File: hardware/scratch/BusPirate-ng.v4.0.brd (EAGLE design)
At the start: 100 x 50 mm, 136 parts, among them CON1 CON-USB-F-MICRO-B, IC10 74LVC1G07DBV, IC11 IC_BUFF_SN74LVC1T45DBV, IC12 74LVC1G07DBV, IC13 IC_BUFF_SN74LVC1T45DBV, IC14 74LVC1G07DBV, IC15 IC_BUFF_SN74LVC1T45DBV, IC16 74LVC1G07DBV, IC17 IC_BUFF_SN74LVC1T45DBV, IC2 IC_MEM_23LC1024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

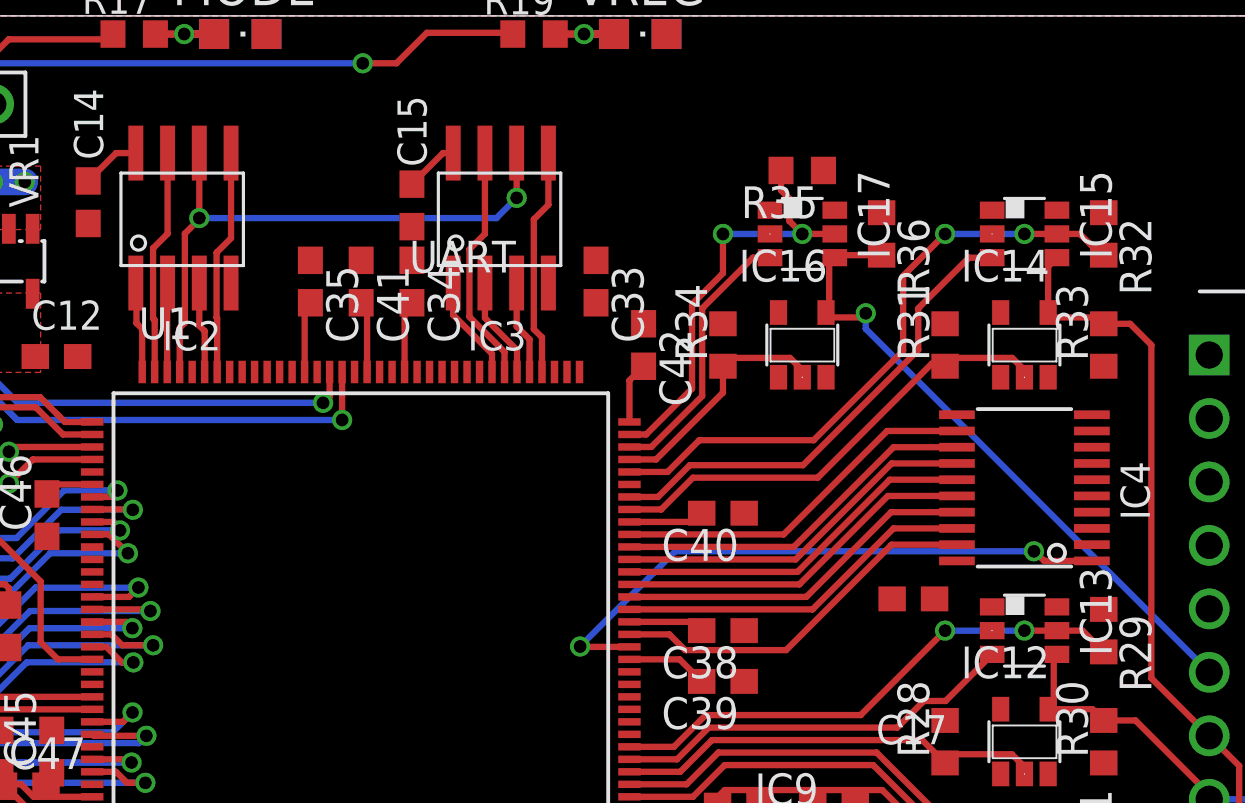
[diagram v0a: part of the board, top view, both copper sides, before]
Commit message: Renamed nets name and wire missing connection -renamed SRAM nets -renamed LATCH nets -wired FSMC control pins. FSMC_NOE_OE, FSMC_NWE_WE and FSMC_NE3_CE to FPGA 11, 12 and 22. -wired PWM pin PC6 (TIM8_CH1/TIM3_CH1) to FPGA 21/GBIN6
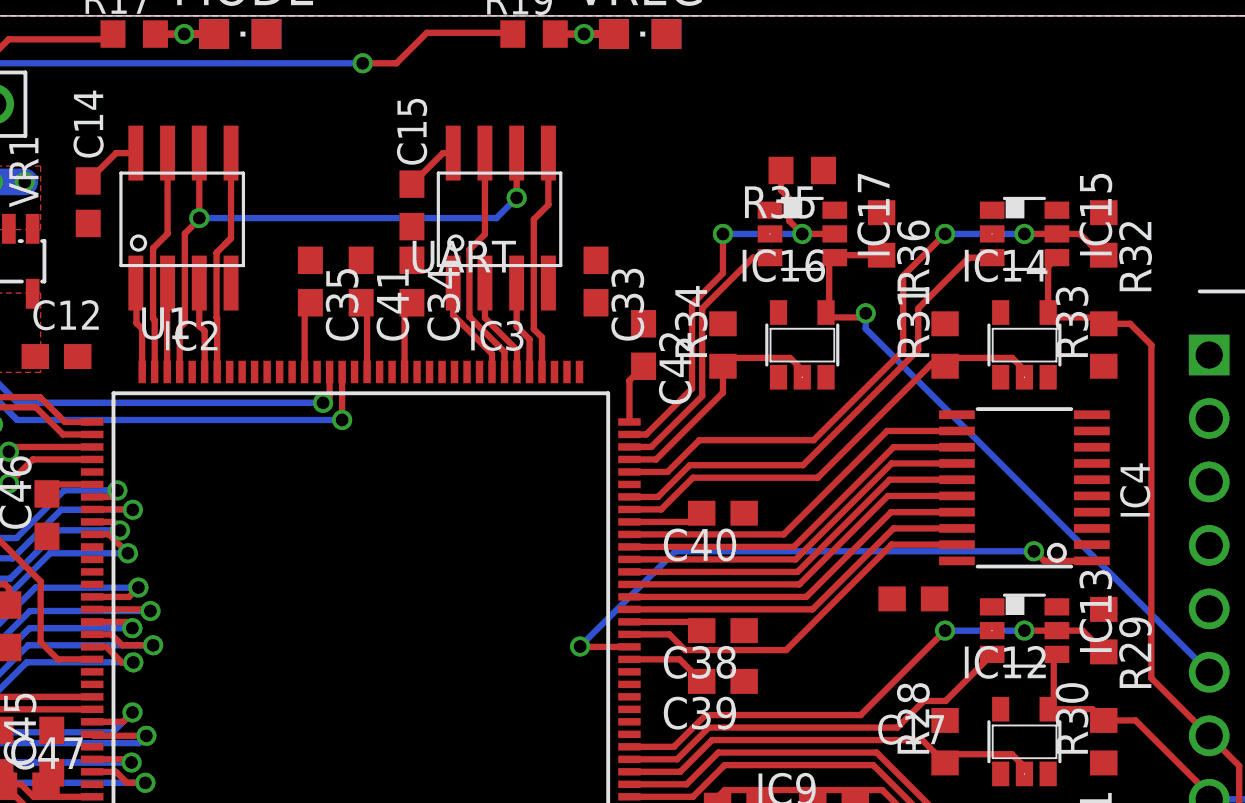
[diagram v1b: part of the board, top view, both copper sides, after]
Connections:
- net IO_OE renamed LAT_OE
- net LA_LAT_AUX0 renamed LAT_AUX0
- net LA_LAT_AUX1 renamed LAT_AUX1
- net LA_LAT_CLK renamed LAT_CLK
- net LA_LAT_CS renamed LAT_CS
- net LA_LAT_MISO renamed LAT_MISO
- net LA_LAT_MOSI renamed LAT_MOSI
- net LA_LAT_SWV33 renamed LAT_SWV33
- net LA_LAT_SWV50 renamed LAT_SWV50
- net LA_MEM_AUX0 renamed SRAM1_SIO0
- net LA_MEM_CLK renamed SRAM0_SIO1
- net LA_MEM_CS renamed SRAM0_SIO3
- net LA_MEM_HOLD renamed SRAM1_SIO3
- net LA_MEM_MISO renamed SRAM0_SIO0
- net LA_MEM_MOSI renamed SRAM0_SIO2
- net LA_MEM_SWV33 renamed SRAM1_SIO1
- net LA_MEM_SWV50 renamed SRAM1_SIO2
- net SRAM_CLK renamed SRAM_CLOCK
- net SRAM_CS1 renamed SRAM0_CS
- net SRAM_CS2 renamed SRAM1_CS
- removed net N$15: U1.11
- removed net N$21: U1.21
- new net N$34: U2.82
- new net N$43: U2.81
- new net N$45: U2.102
- new net N$46: U2.101
- new net N$47: U2.110
- new net N$50: U2.88
- new net N$51: U2.89
- new net N$52: U2.90
- new net N$53: U2.93
- new net N$54: U2.124
- new net PWM: U1.21, U2.96
- net FSMC_NE3_CE: now also U1.22
- net FSMC_NOE_OE: now also U1.11
- net FSMC_NWE_WE: now also U1.12
- net N$19: now also U2.97; no longer U1.12
- net N$22: now also U2.98; no longer U1.22

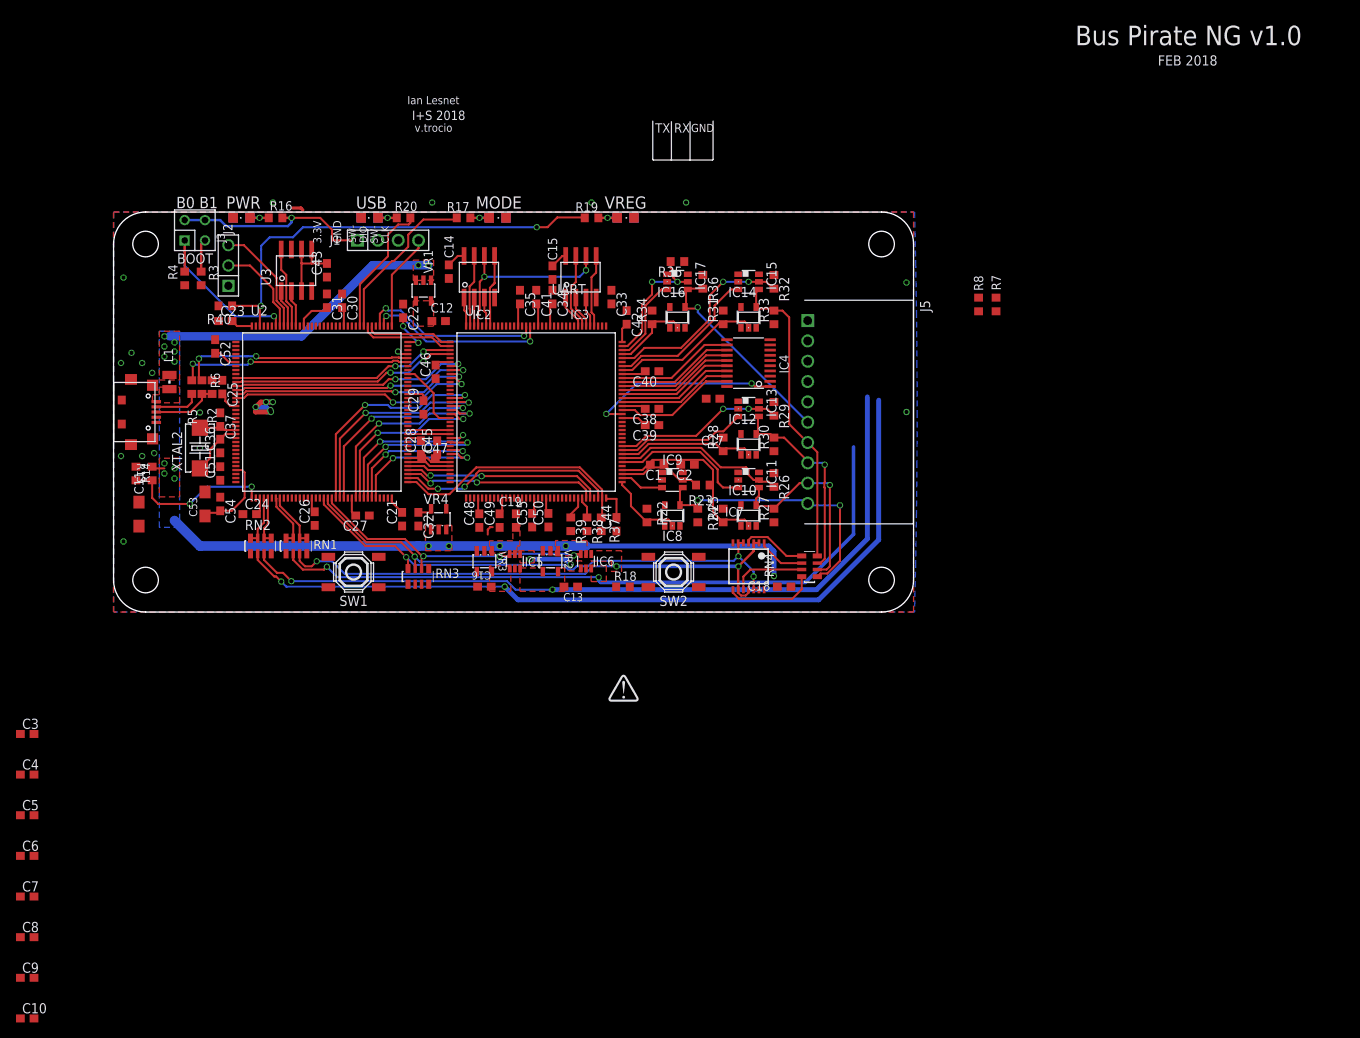
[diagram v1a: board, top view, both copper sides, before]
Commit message: Continued routing, swapped some pins on FPGA swapped FPGA pins: BUFOD_CLOCK with BUFOD_MOSI BUFIO_CLOCK with BUFIO_MOSI BUFDIR_CLOCK with BUFDIR_MOSI BUFDIR_AUX with BUFDIR_CS BUFIO_AUX with BUFIO_CS BUFOD_AUX with BUFOD_CS
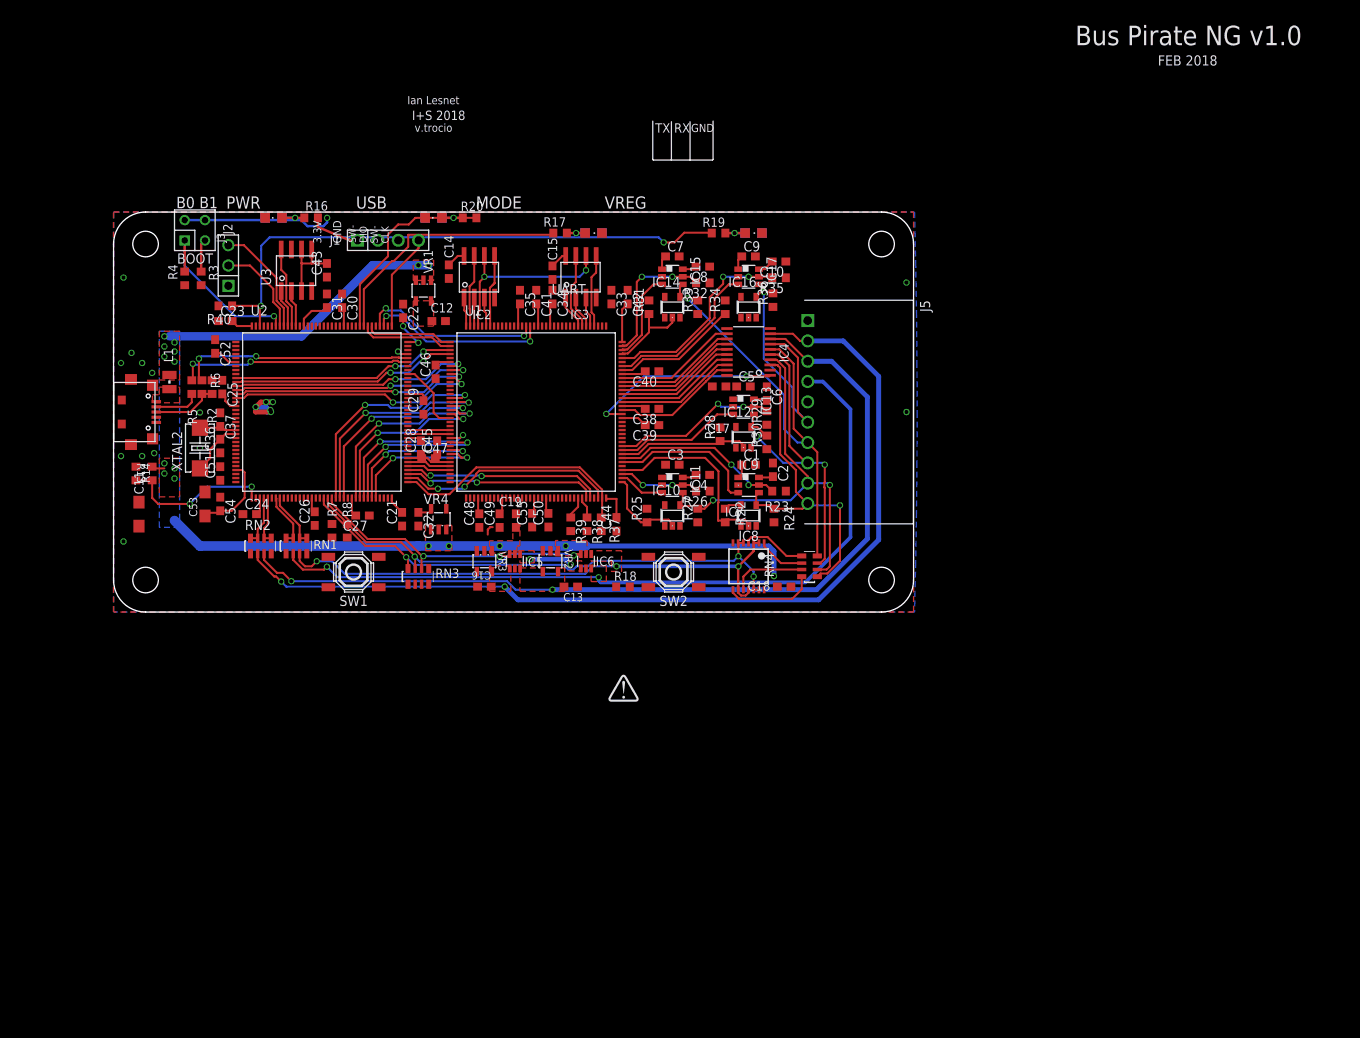
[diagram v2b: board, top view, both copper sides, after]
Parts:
- moved C10 133.4 mm to (83.2, 43.8), turned to 180 degrees
- moved C9 127.5 mm to (79.4, 44.5)
- moved C8 119.0 mm to (73.7, 43.2), turned to 180 degrees
- moved C7 113.6 mm to (69.8, 44.5)
- moved C6 109.0 mm to (81.7, 27.3), turned to 270 degrees
- moved C5 104.3 mm to (78.7, 28.2)
- moved C4 92.4 mm to (73.7, 17.1), turned to 180 degrees
- moved R7 87.7 mm to (27.3, 10.2)
- moved C3 87.4 mm to (69.8, 18.4)
- moved R8 83.8 mm to (29.2, 10.2)
- moved LED5 16.1 mm to (80.0, 47.4)
- moved LED6 16.1 mm to (80.0, 47.4)
- moved R19 16.0 mm to (75.6, 47.4)
- moved R35 12.9 mm to (83.2, 41.8)
- moved R17 12.2 mm to (55.8, 47.4)
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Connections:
- net BUFDIR_AUX: now also U1.104; no longer U1.107
- net BUFDIR_CLOCK: now also U1.75; no longer U1.79
- net BUFDIR_CS: now also U1.107; no longer U1.104
- net BUFDIR_MOSI: now also U1.79; no longer U1.75
- net BUFIO_AUX: now also U1.102; no longer U1.106
- net BUFIO_CLOCK: now also U1.74; no longer U1.78
- net BUFIO_CS: now also U1.106; no longer U1.102
- net BUFIO_MOSI: now also U1.78; no longer U1.74
- net BUFOD_AUX: now also U1.101; no longer U1.105
- net BUFOD_CLOCK: now also U1.73; no longer U1.76
- net BUFOD_CS: now also U1.105; no longer U1.101
- net BUFOD_MOSI: now also U1.76; no longer U1.73
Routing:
- net BPIO_CLOCK: track 25.0 -> 51.8 mm
- net BPIO_CS: track 38.3 -> 58.1 mm, vias 0 -> 1
- net BPIO_MISO: track 25.6 -> 44.5 mm, vias 1 -> 2
- net SWV50: track 101.0 -> 119.8 mm
- net VREGEN: track 55.7 -> 71.3 mm
- net SWV33: track 98.1 -> 113.2 mm
- net BUFOD_MOSI: track 9.98 -> 24.5 mm
- net BUFIO_MOSI: track 5.48 -> 18.6 mm
- net BUFOD_CLOCK: track 23.3 -> 10.7 mm
- net BUFIO_CLOCK: track 17.8 -> 5.75 mm
- net BUFDIR_CLOCK: track 22.0 -> 10.1 mm, vias 0 -> 2
- net BUFDIR_MOSI: track 10.5 -> 22.2 mm, vias 0 -> 2
- net VEXTERN: track 85.9 -> 97.3 mm
- net LD1: track 20.8 -> 32.1 mm
- net 3V3: track 117.9 -> 127.5 mm
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
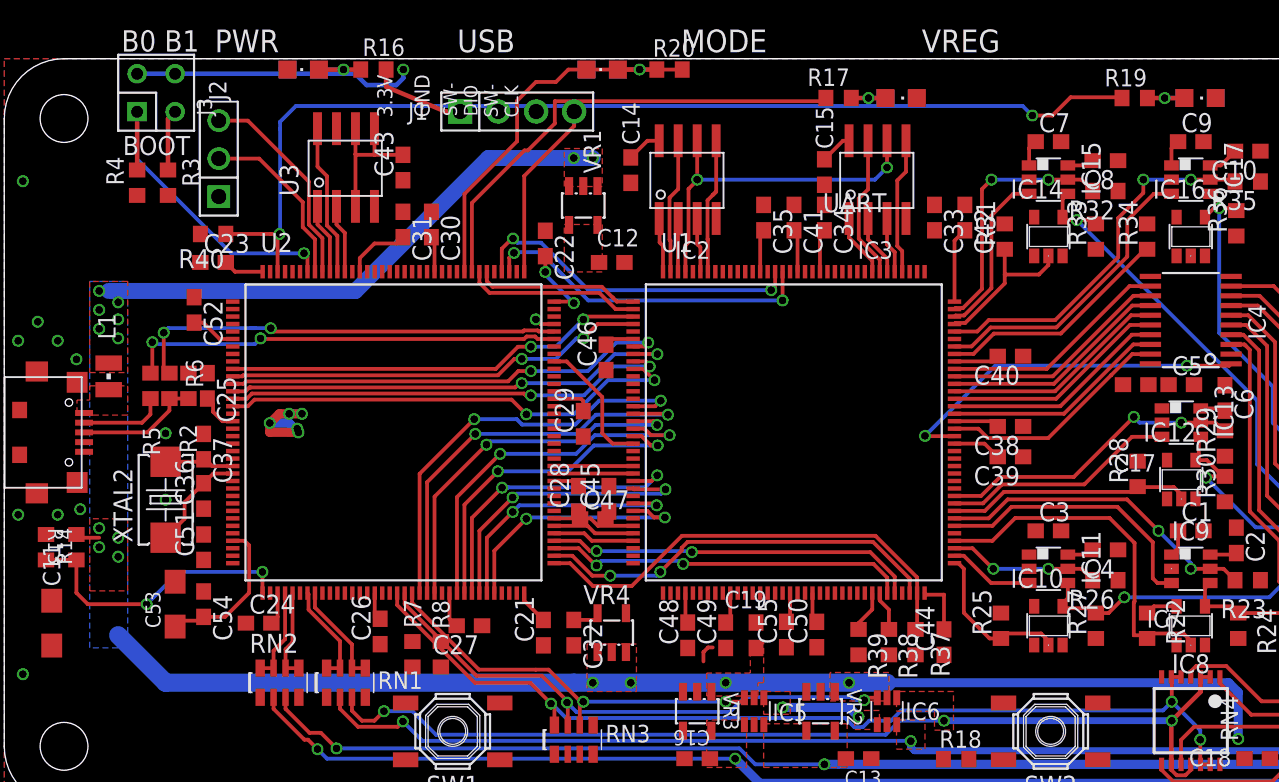
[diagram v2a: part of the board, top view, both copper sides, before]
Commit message: move some pins, wire vrefs, change caps size and continue routing -wire vref+ and vref- to 3.3V and GND -wired MCU_INT0 to PE2 and MCU_INT1 to PE3, to have each pin a dedicated interrupt. -change capacitor size from 0604 to 0402 capacitors C20, C45 and C47 -moved USB_DET from PF11 to PE4
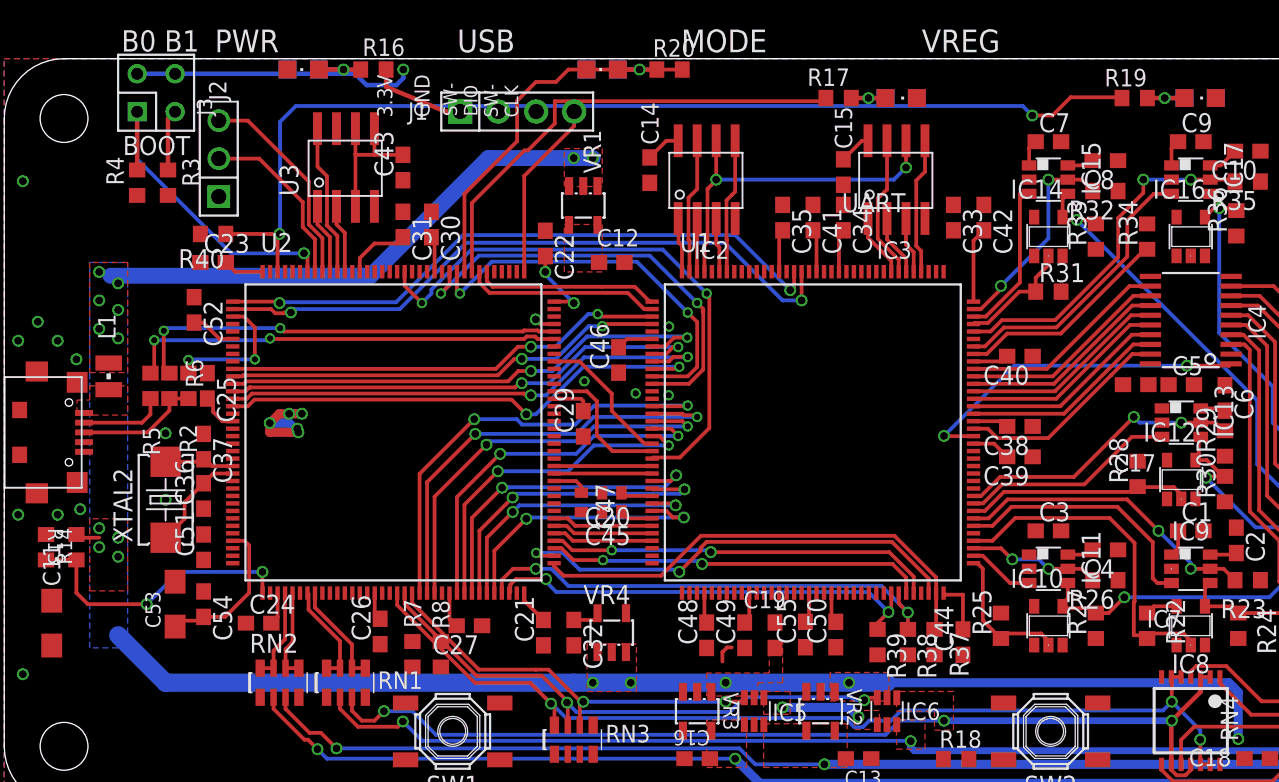
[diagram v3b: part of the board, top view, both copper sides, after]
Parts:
- removed C28: 0.1uF, rcl:C0603
- added C20: 0.1uF, dp_devices.v6:C402
- C45, C47: device rcl:C0603 -> dp_devices.v6:C402
- moved R31 4.70 mm to (69.8, 34.4), turned to 0 degrees
- moved C47 1.33 mm to (38.6, 20.3), turned to 270 degrees
- moved C14 1.27 mm to (43.2, 42.5)
- moved C15 1.27 mm to (56.1, 42.4)
- moved C33 1.27 mm to (63.5, 39.4)
- moved C34 1.27 mm to (56.1, 39.4)
- moved C35 1.27 mm to (52.1, 39.4)
- moved C44 1.27 mm to (64.1, 11.0)
- moved C48 1.27 mm to (47.0, 11.4)
- moved C49 1.27 mm to (49.5, 11.4)
- moved C55 1.27 mm to (53.6, 11.5)
- moved IC2 1.27 mm to (47.0, 41.9)
- moved R39 1.27 mm to (58.4, 11.0)
- moved U1 1.27 mm to (54.1, 25.0)
- moved C19 1.27 mm to (51.6, 11.4)
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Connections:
- removed net N$27: U2.1
- net 1V2: now also C20.1; no longer C45.2
- net 3V3: now also C45.1, C47.1, U2.32; no longer C28.2, C47.2
- net GND: now also C20.2, C45.2, C47.2, U2.31; no longer C28.1, C45.1, C47.1
- net MCU_INT0: now also U2.1; no longer U2.112
- net MCU_INT1: now also U2.2; no longer U2.111
- net USB_DET: now also U2.3; no longer U2.49
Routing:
- net FSMC_NE3_CE: track 0.00 -> 38.2 mm, vias 0 -> 2
- net FSMC_NWE_WE: track 0.00 -> 29.8 mm, vias 0 -> 2
- net FPGA_CRESET: track 2.68 -> 32.2 mm, vias 0 -> 2
- net FPGA_CDONE: track 2.81 -> 29.9 mm, vias 0 -> 2
- net FSMC_NOE_OE: track 0.00 -> 26.3 mm, vias 0 -> 2
- net MCU_INT1: track 22.6 -> 43.6 mm
- net MCU_INT0: track 22.6 -> 42.1 mm
- net PWM: track 0.00 -> 9.55 mm
- net USB_DET: track 0.00 -> 9.26 mm, vias 0 -> 2
- net FSMC_A2: track 30.1 -> 34.4 mm
- net FSMC_A4: track 30.2 -> 34.2 mm
- net FPGA_PROG_CLOCK: track 27.4 -> 31.0 mm
- net BUFOD_CS: track 11.0 -> 7.80 mm
- net FSMC_D6: track 25.1 -> 27.9 mm
- net BUFDIR_CS: track 17.2 -> 14.4 mm
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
